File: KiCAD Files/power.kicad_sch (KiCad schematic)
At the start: 2 parts, among them U1 K230_Rewired, U5 RT9992ZQW

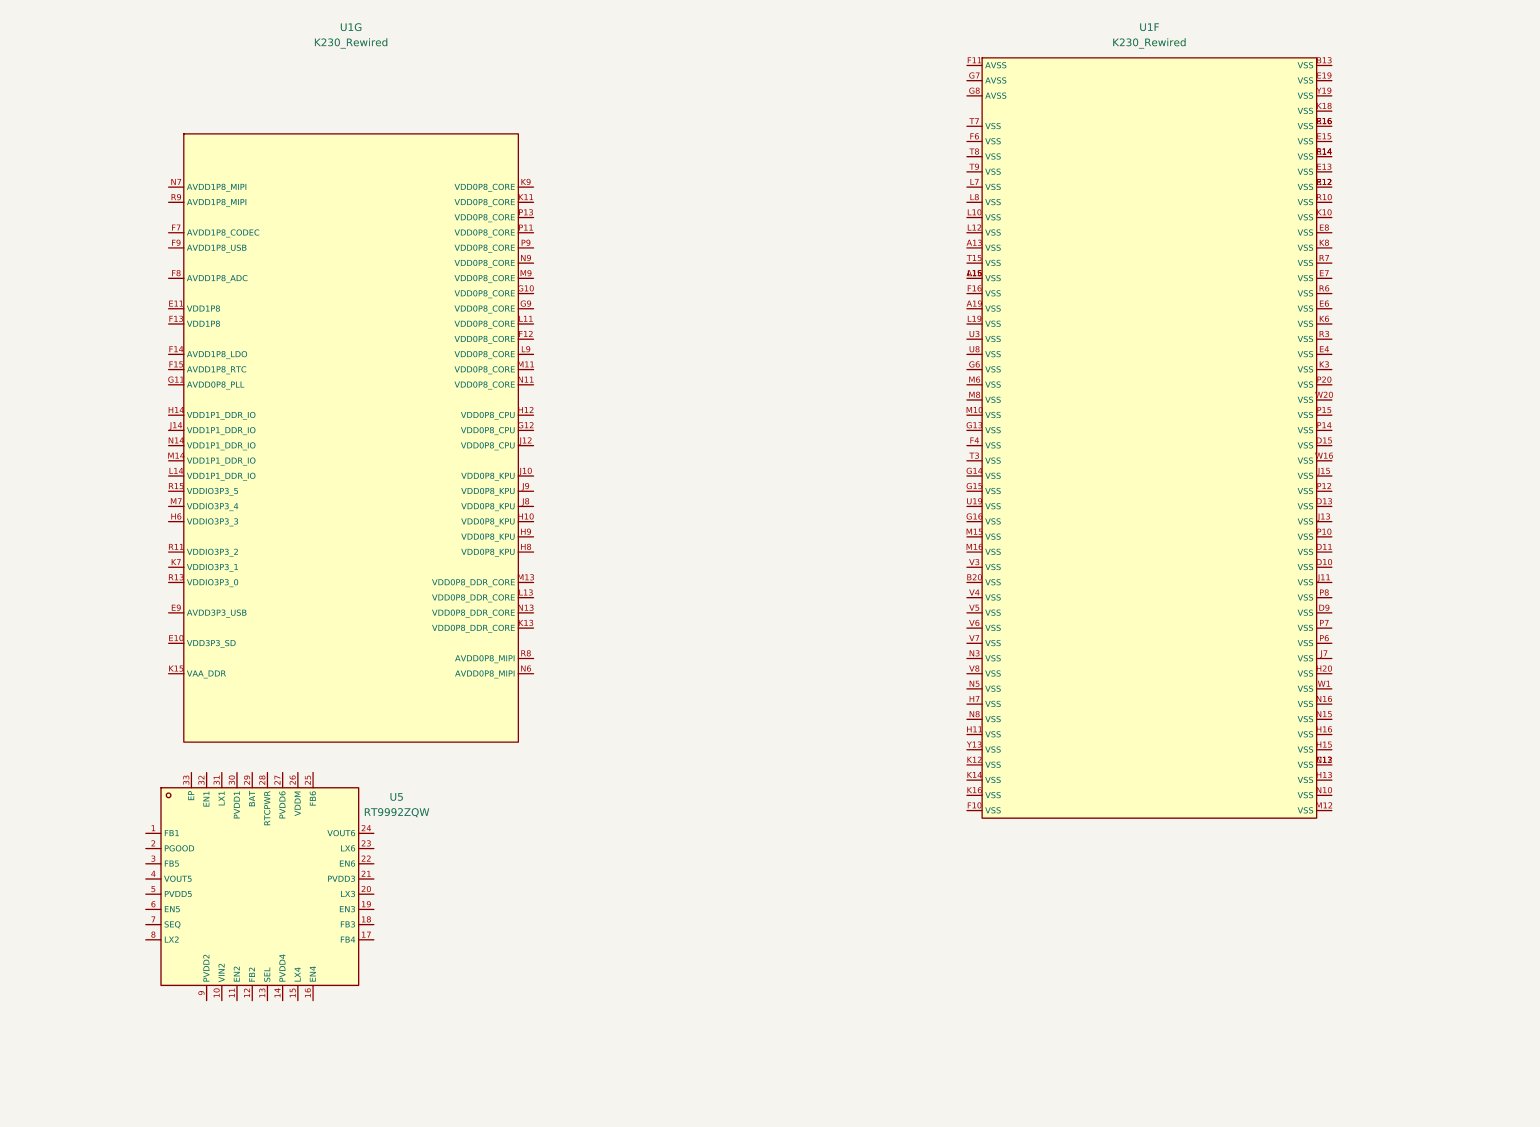
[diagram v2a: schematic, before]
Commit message: schematic is pretty much done
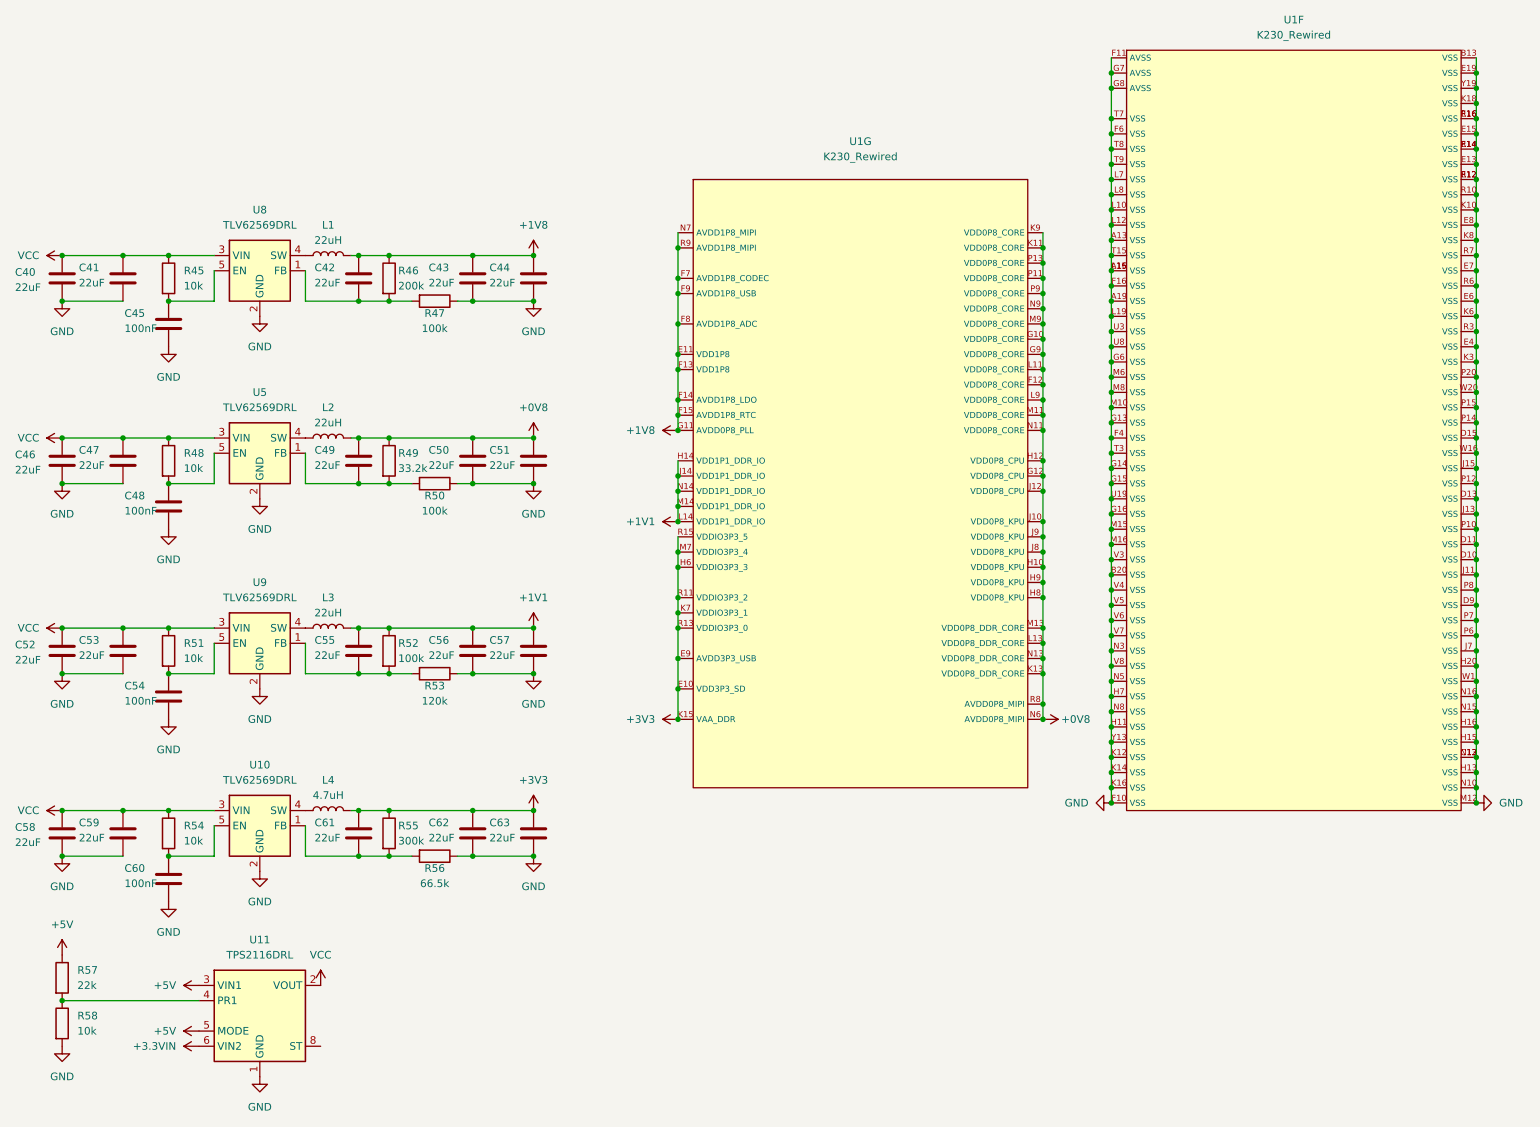
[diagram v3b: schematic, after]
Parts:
- removed U5: RT9992ZQW, Package_DFN_QFN:Texas_RSN_WQFN-32-1EP_4x4mm_P0.4mm_EP2.8x2.8mm, symbol LCSC:RT9992ZQW
- added C40, C41, C42, C43, C44, C46, C47, C49, C50, C51, C52, C53, C55, C56, C57, C58, C59, C61, C62, C63: 22uF, Capacitor_SMD:C_0402_1005Metric, symbol Device:C
- added C45, C48, C54, C60: 100nF, Capacitor_SMD:C_0402_1005Metric, symbol Device:C
- added L1, L2, L3: 22uH, Inductor_SMD:L_APV_APH0620, symbol Device:L
- added L4: 4.7uH, Inductor_SMD:L_APV_APH0620, symbol Device:L
- added R45, R48, R51, R54, R58: 10k, symbol Device:R
- added R46: 200k, symbol Device:R
- added R47, R50, R52: 100k, symbol Device:R
- added R49: 33.2k, symbol Device:R
- added R53: 120k, symbol Device:R
- added R55: 300k, symbol Device:R
- added R56: 66.5k, symbol Device:R
- added R57: 22k, symbol Device:R
- added U10, U5, U8, U9: TLV62569DRL, Package_TO_SOT_SMD:SOT-563, symbol Regulator_Switching:TLV62569DRL
- added U11: TPS2116DRL, Package_TO_SOT_SMD:SOT-583-8, symbol Power_Management:TPS2116DRL
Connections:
- net +3V3: now reaches U1.E10 (VDD3P3_SD)
- net +3V3: now also U1.E9 (AVDD3P3_USB), U1.H6 (VDDIO3P3_3), U1.K15 (VAA_DDR), U1.K7 (VDDIO3P3_1), U1.M7 (VDDIO3P3_4), U1.R11 (VDDIO3P3_2), U1.R13 (VDDIO3P3_0), U1.R15 (VDDIO3P3_5), C61.1, C62.1, C63.1, L4.2, R55.1
- net +1V8: now reaches U1.E11 (VDD1P8)
- net +1V8: now also U1.F13 (VDD1P8), U1.F14 (AVDD1P8_LDO), U1.F15 (AVDD1P8_RTC), U1.F7 (AVDD1P8_CODEC), U1.F8 (AVDD1P8_ADC), U1.F9 (AVDD1P8_USB), U1.G11 (AVDD0P8_PLL), U1.N7 (AVDD1P8_MIPI), U1.R9 (AVDD1P8_MIPI), C42.1, C43.1, C44.1, L1.2, R46.1
- net +0V8: now reaches U1.F12 (VDD0P8_CORE)
- net +0V8: now also U1.G10 (VDD0P8_CORE), U1.G12 (VDD0P8_CPU), U1.G9 (VDD0P8_CORE), U1.H10 (VDD0P8_KPU), U1.H12 (VDD0P8_CPU), U1.H8 (VDD0P8_KPU), U1.H9 (VDD0P8_KPU), U1.J10 (VDD0P8_KPU), U1.J12 (VDD0P8_CPU), U1.J8 (VDD0P8_KPU), U1.J9 (VDD0P8_KPU), U1.K11 (VDD0P8_CORE), U1.K13 (VDD0P8_DDR_CORE), U1.K9 (VDD0P8_CORE), U1.L11 (VDD0P8_CORE), U1.L13 (VDD0P8_DDR_CORE), U1.L9 (VDD0P8_CORE), U1.M11 (VDD0P8_CORE), U1.M13 (VDD0P8_DDR_CORE), U1.M9 (VDD0P8_CORE), U1.N11 (VDD0P8_CORE), U1.N13 (VDD0P8_DDR_CORE), U1.N6 (AVDD0P8_MIPI), U1.N9 (VDD0P8_CORE), U1.P11 (VDD0P8_CORE), U1.P13 (VDD0P8_CORE), U1.P9 (VDD0P8_CORE), U1.R8 (AVDD0P8_MIPI), C49.1, C50.1, C51.1, L2.2, R49.1
- net +1V1: now reaches U1.H14 (VDD1P1_DDR_IO)
- net +1V1: now also U1.J14 (VDD1P1_DDR_IO), U1.L14 (VDD1P1_DDR_IO), U1.M14 (VDD1P1_DDR_IO), U1.N14 (VDD1P1_DDR_IO), C55.1, C56.1, C57.1, L3.2, R52.1
- net GND: now reaches U1.A13 (VSS)
- net GND: now also U1.A16 (VSS), U1.A19 (VSS), U1.B13 (VSS), U1.B20 (VSS), U1.C13 (VSS), U1.D10 (VSS), U1.D11 (VSS), U1.D13 (VSS), U1.D15 (VSS), U1.D9 (VSS), U1.E12 (VSS), U1.E13 (VSS), U1.E14 (VSS), U1.E15 (VSS), U1.E16 (VSS), U1.E19 (VSS), U1.E4 (VSS), U1.E6 (VSS), U1.E7 (VSS), U1.E8 (VSS), U1.F10 (VSS), U1.F11 (AVSS), U1.F16 (VSS), U1.F4 (VSS), U1.F6 (VSS), U1.G13 (VSS), U1.G14 (VSS), U1.G15 (VSS), U1.G16 (VSS), U1.G6 (VSS), U1.G7 (AVSS), U1.G8 (AVSS), U1.H11 (VSS), U1.H13 (VSS), U1.H15 (VSS), U1.H16 (VSS), U1.H20 (VSS), U1.H7 (VSS), U1.J11 (VSS), U1.J13 (VSS), U1.J15 (VSS), U1.J7 (VSS), U1.K10 (VSS), U1.K12 (VSS), U1.K14 (VSS), U1.K16 (VSS), U1.K18 (VSS), U1.K3 (VSS), U1.K6 (VSS), U1.K8 (VSS), U1.L10 (VSS), U1.L12 (VSS), U1.L15 (VSS), U1.L19 (VSS), U1.L7 (VSS), U1.L8 (VSS), U1.M10 (VSS), U1.M12 (VSS), U1.M15 (VSS), U1.M16 (VSS), U1.M6 (VSS), U1.M8 (VSS), U1.N10 (VSS), U1.N12 (VSS), U1.N15 (VSS), U1.N16 (VSS), U1.N3 (VSS), U1.N5 (VSS), U1.N8 (VSS), U1.P10 (VSS), U1.P12 (VSS), U1.P14 (VSS), U1.P15 (VSS), U1.P20 (VSS), U1.P6 (VSS), U1.P7 (VSS), U1.P8 (VSS), U1.R10 (VSS), U1.R12 (VSS), U1.R14 (VSS), U1.R16 (VSS), U1.R3 (VSS), U1.R6 (VSS), U1.R7 (VSS), U1.T15 (VSS), U1.T3 (VSS), U1.T7 (VSS), U1.T8 (VSS), U1.T9 (VSS), U1.U19 (VSS), U1.U3 (VSS), U1.U8 (VSS), U1.V3 (VSS), U1.V4 (VSS), U1.V5 (VSS), U1.V6 (VSS), U1.V7 (VSS), U1.V8 (VSS), U1.W1 (VSS), U1.W16 (VSS), U1.W20 (VSS), U1.Y13 (VSS), U1.Y19 (VSS), C40.2, C41.2, C43.2, C44.2, C45.2, C46.2, C47.2, C48.2, C50.2, C51.2, C52.2, C53.2, C54.2, C56.2, C57.2, C58.2, C59.2, C60.2, C62.2, C63.2, R47.1, R50.1, R53.1, R56.1, R58.2, U10.2 (GND), U11.1 (GND), U5.2 (GND), U8.2 (GND), U9.2 (GND)
- new net: C61.2, R55.2, R56.2, U10.1 (FB)
- new net: C42.2, R46.2, R47.2, U8.1 (FB)
- new net: C55.2, R52.2, R53.2, U9.1 (FB)
- new net: C49.2, R49.2, R50.2, U5.1 (FB)
- new net: L2.1, U5.4 (SW)
- new net: C48.1, R48.2, U5.5 (EN)
- new net: C45.1, R45.2, U8.5 (EN)
- new net: C60.1, R54.2, U10.5 (EN)
- new net: L3.1, U9.4 (SW)
- new net: R57.2, R58.1, U11.4 (PR1)
- new net: C54.1, R51.2, U9.5 (EN)
- new net: L1.1, U8.4 (SW)
- new net: L4.1, U10.4 (SW)
- new net +3.3VIN: U11.6 (VIN2)
- new net +5V: R57.1, U11.3 (VIN1), U11.5 (MODE)
- new net VCC: C40.1, C41.1, C46.1, C47.1, C52.1, C53.1, C58.1, C59.1, R45.1, R48.1, R51.1, R54.1, U10.3 (VIN), U11.2 (VOUT), U11.7 (VOUT), U5.3 (VIN), U8.3 (VIN), U9.3 (VIN)
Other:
- moved on the sheet: U1F, U1G
